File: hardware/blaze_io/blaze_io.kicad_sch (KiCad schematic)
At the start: 50 parts, among them J1 Conn_01x04, J2 Conn_01x04, J3 JTAG, Q1 AO4892, Q2 AO4892, SW1 SW_SPST, SW2 SW_SPDT, U1 TCAN1044VDDFR, U2 STM32H503KBUx

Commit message: Connected IO, wrote docs
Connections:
- net FET_A: now also U2.6 (PA0)
- net FET_A_SENSE: now also U2.10 (PA4)
- net FET_B: now also U2.7 (PA1)
- net FET_B_SENSE: now also U2.11 (PA5)
- net FET_C: now also U2.8 (PA2)
- net FET_C_SENSE: now also U2.12 (PA6)
- net FET_D: now also U2.9 (PA3)
- net FET_D_SENSE: now also U2.13 (PA7)
- no-connect marks 17 -> 11

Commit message: Updated IO title block
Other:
- company: (none) -> UCSC Rocket Team
- title: (none) -> Blaze IO
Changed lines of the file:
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@@
 	(generator_version "8.0")
 	(paper "A4")
+	(title_block
+		(title "Blaze IO")
+		(date "2024-09-19")
+		(rev "1")
+		(company "UCSC Rocket Team")
+		(comment 1 "Designed by Julian Barbera")
+	)

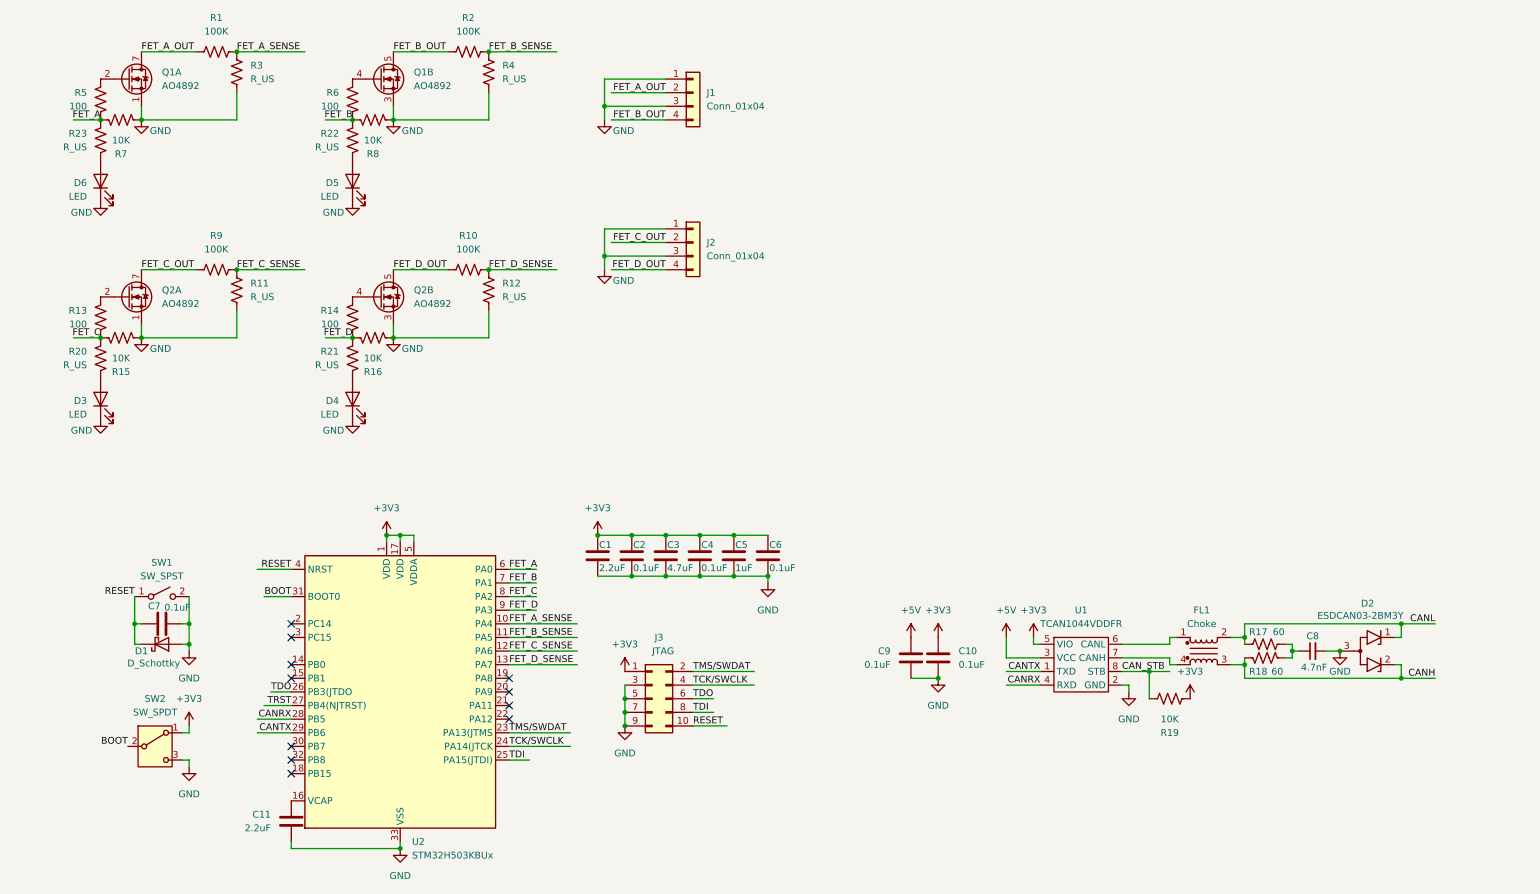
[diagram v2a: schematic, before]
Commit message: Added ARM AND gates to IO board
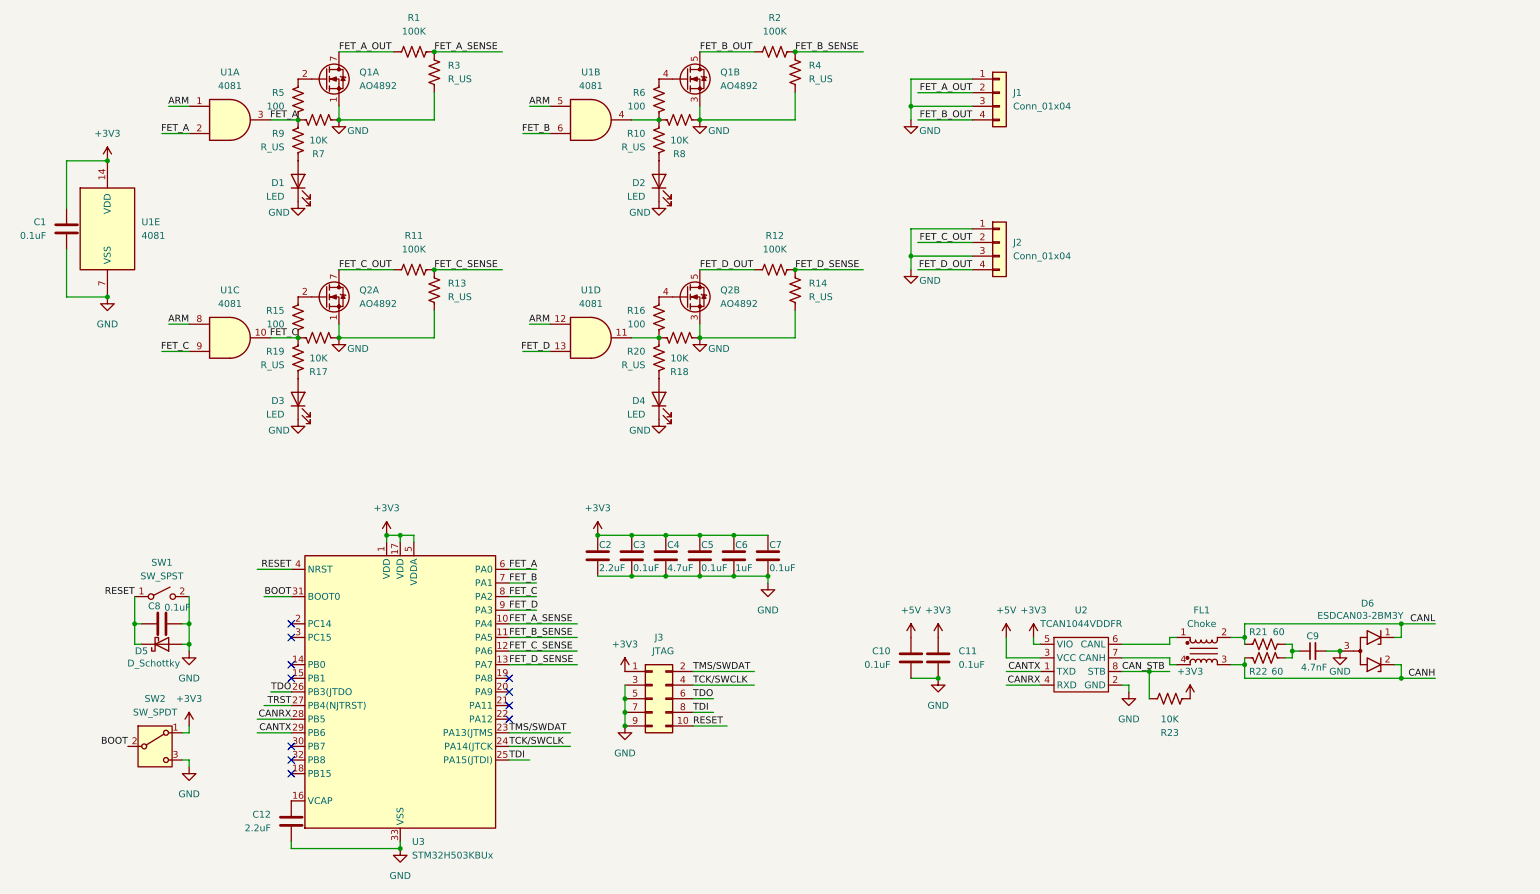
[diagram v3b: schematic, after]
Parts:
- added C1: 0.1uF, symbol Device:C
- added U1: 4081, symbol 4xxx:4081
- renumbered C9 to C10, C10 to C11, C11 to C12, C1 to C2, C2 to C3, C3 to C4, C4 to C5, C5 to C6, C6 to C7, C7 to C8, C8 to C9, D6 to D1, D5 to D2, D1 to D5, D2 to D6, R22 to R10, R9 to R11, R10 to R12, R11 to R13, R12 to R14, R13 to R15, R14 to R16, R15 to R17, R16 to R18, R20 to R19, R21 to R20, R17 to R21, R18 to R22, R19 to R23, R23 to R9, U1 to U2, U2 to U3
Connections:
- net +3V3: now also C1.1, U1.14 (VDD)
- net FET_A: now also U1.2, U1.3
- net FET_B: now also U1.6; no longer R10.1, R6.2, R8.1
- net FET_C: now also U1.10, U1.9
- net FET_D: now also U1.13; no longer R16.2, R18.1, R20.1
- net GND: now also C1.2, U1.7 (VSS)
- new net: R16.2, R18.1, R20.1, U1.11
- new net: R10.1, R6.2, R8.1, U1.4
- new net ARM: U1.1, U1.12, U1.5, U1.8
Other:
- moved on the sheet: D1, D2, D3, D4, J1, J2, Q1A, Q1B, Q2A, Q2B, R1, R10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

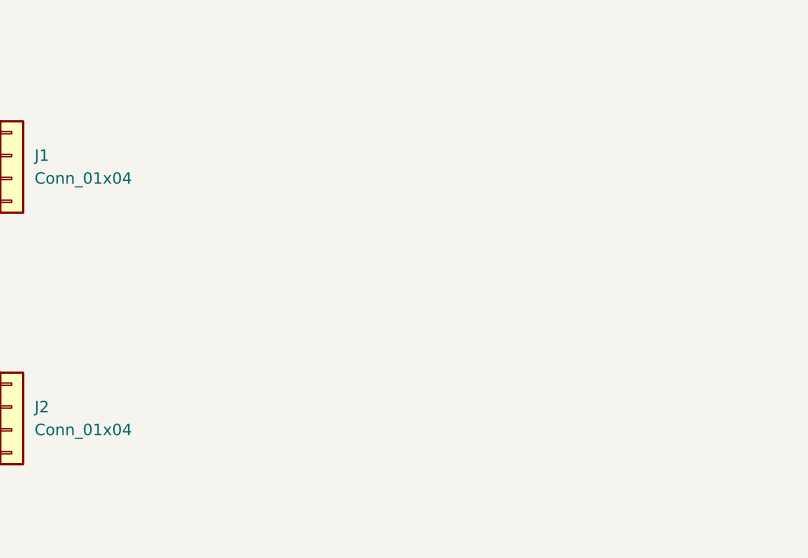
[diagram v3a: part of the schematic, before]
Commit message: Added servo outputs
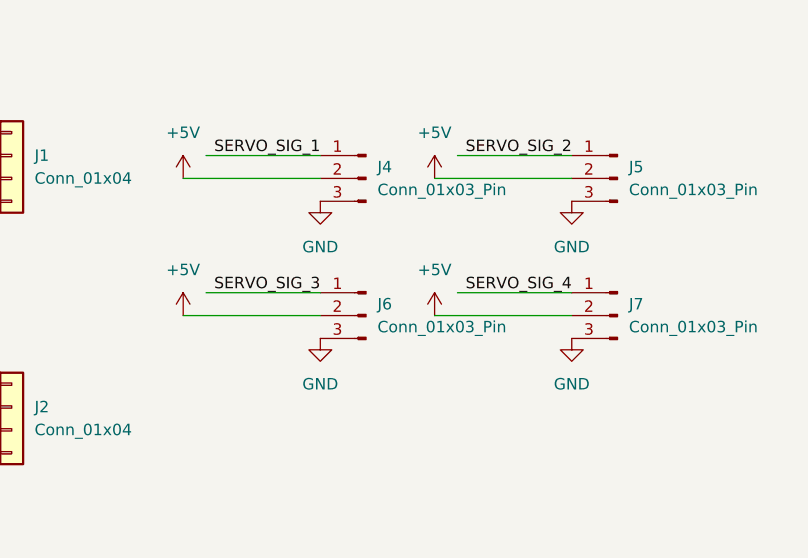
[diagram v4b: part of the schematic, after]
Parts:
- added J4, J5, J6, J7: Conn_01x03_Pin, symbol Connector:Conn_01x03_Pin
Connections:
- net +5V: now also J4.2 (Pin_2), J5.2 (Pin_2), J6.2 (Pin_2), J7.2 (Pin_2)
- net GND: now also J4.3 (Pin_3), J5.3 (Pin_3), J6.3 (Pin_3), J7.3 (Pin_3)
- new net SERVO_SIG_1: J4.1 (Pin_1)
- new net SERVO_SIG_2: J5.1 (Pin_1)
- new net SERVO_SIG_3: J6.1 (Pin_1)
- new net SERVO_SIG_4: J7.1 (Pin_1)

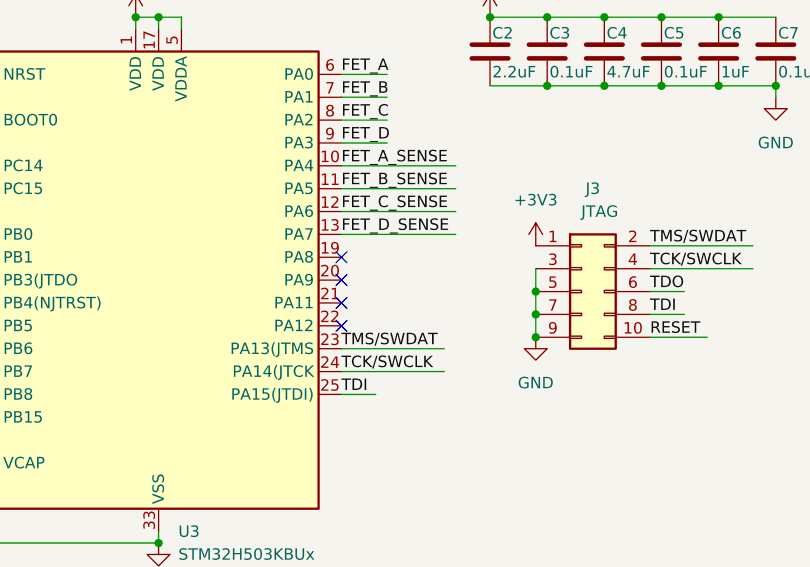
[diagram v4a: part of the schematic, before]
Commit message: Added PWM outputs to microcontroller
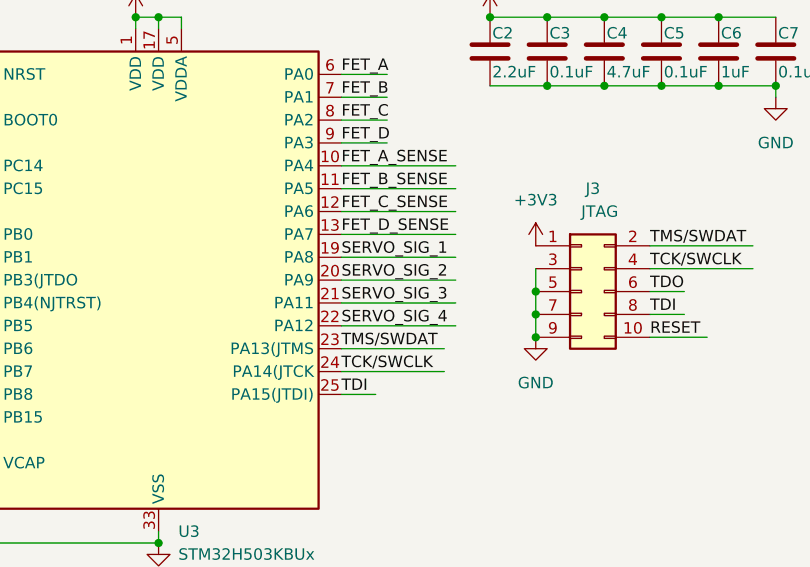
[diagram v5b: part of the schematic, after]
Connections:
- net SERVO_SIG_1: now also U3.19 (PA8)
- net SERVO_SIG_2: now also U3.20 (PA9)
- net SERVO_SIG_3: now also U3.21 (PA11)
- net SERVO_SIG_4: now also U3.22 (PA12)
- no-connect marks 11 -> 7

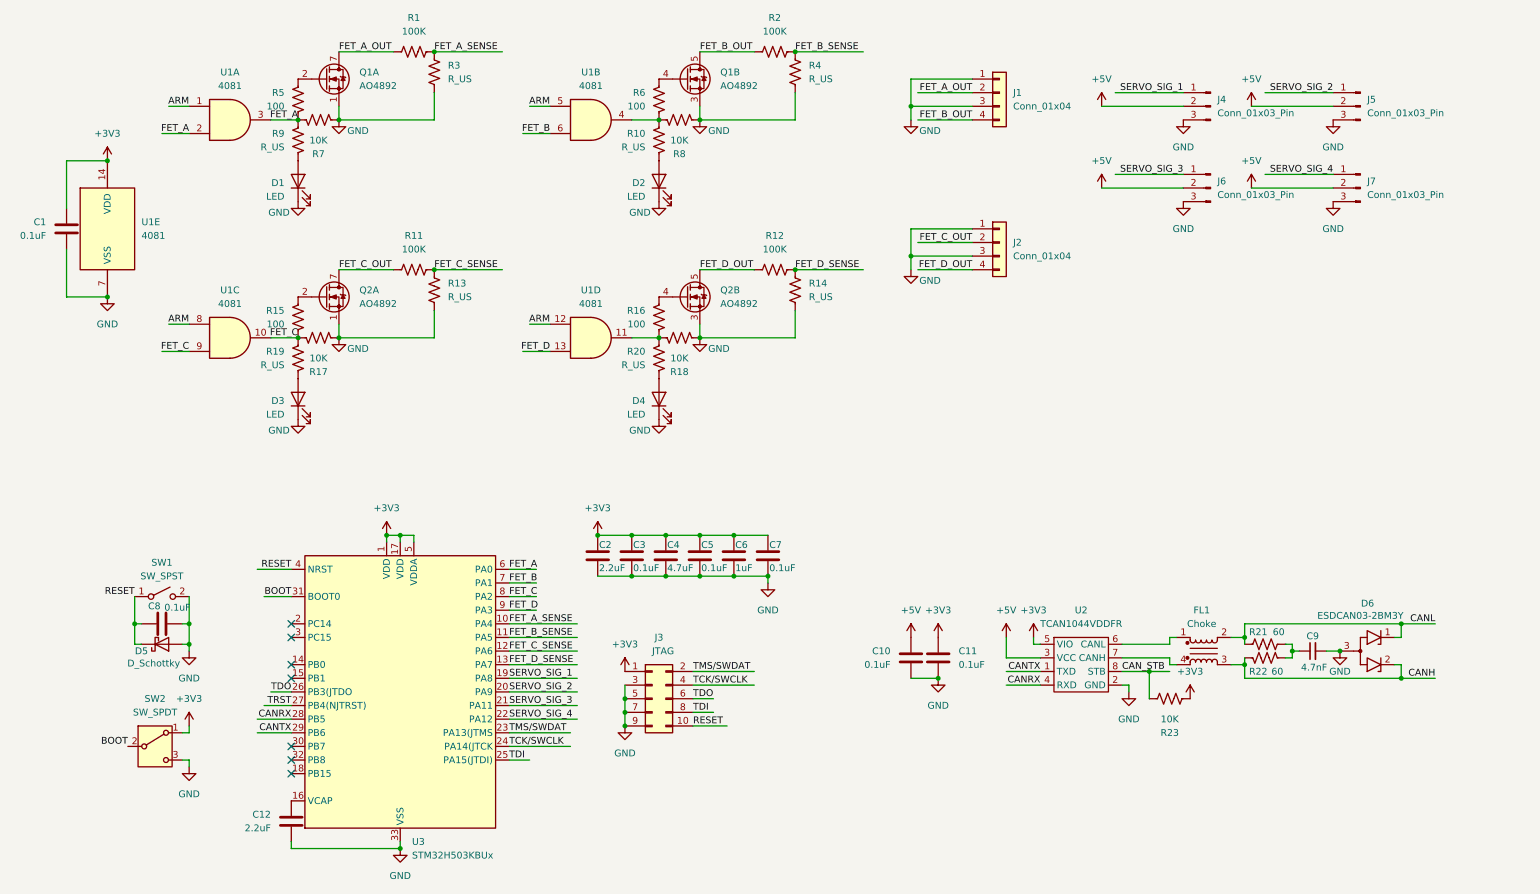
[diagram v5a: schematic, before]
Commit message: Removed audio, neopixel, can2 from interconnect
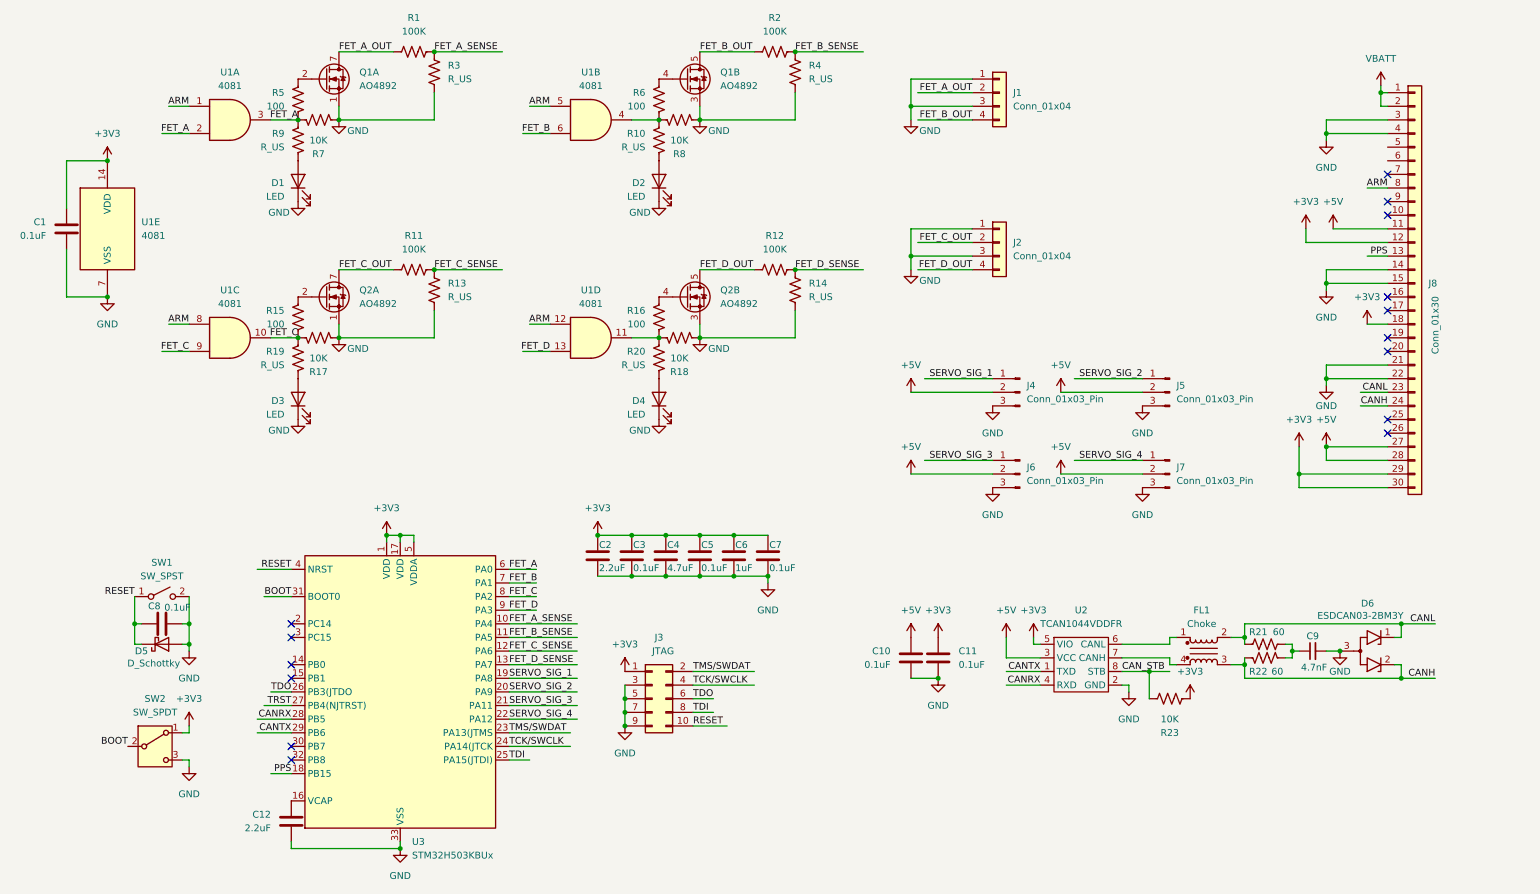
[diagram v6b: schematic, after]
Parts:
- added J8: Conn_01x30, symbol Connector_Generic:Conn_01x30
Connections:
- net +3V3: now also J8.12 (Pin_12), J8.18 (Pin_18), J8.29 (Pin_29), J8.30 (Pin_30)
- net +5V: now also J8.11 (Pin_11), J8.27 (Pin_27), J8.28 (Pin_28)
- net ARM: now also J8.8 (Pin_8)
- net CANH: now also J8.24 (Pin_24)
- net CANL: now also J8.23 (Pin_23)
- net GND: now also J8.14 (Pin_14), J8.15 (Pin_15), J8.21 (Pin_21), J8.22 (Pin_22), J8.3 (Pin_3), J8.4 (Pin_4)
- net PPS: now reaches U3.18 (PB15)
- net PPS: now also J8.13 (Pin_13)
- new net VBATT: J8.1 (Pin_1), J8.2 (Pin_2)
- no-connect marks 7 -> 15
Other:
- moved on the sheet: J4, J5, J6, J7

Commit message: IO Footprint Assignments
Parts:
- C1, C10, C11, C12, C2, C3, C4, C5, C6, C7, C8, C9: footprint (none) -> Capacitor_SMD:C_0603_1608Metric
- D1, D2, D3, D4: footprint (none) -> LED_SMD:LED_0603_1608Metric
- D5: footprint (none) -> Diode_SMD:D_0603_1608Metric
- J3: footprint (none) -> Connector_PinHeader_1.00mm:PinHeader_2x05_P1.00mm_Vertical_SMD
- J8: footprint (none) -> DF17:HRS_DF17_1.0H_-30DP-0.5V_57_
- R1, R10, R11, R12, R13, R14, R15, R16, R17, R18, R19, R2, R20, R21, R22, R23, R3, R4, R5, R6, R7, R8, R9: footprint (none) -> Resistor_SMD:R_0603_1608Metric
- SW1: footprint (none) -> Button_Switch_SMD:SW_SPST_B3U-1000P
- SW2: footprint (none) -> Button_Switch_SMD:Nidec_Copal_CAS-120A
- U2: footprint (none) -> Package_SON:Texas_VSON-HR-8_1.5x2mm_P0.5mm

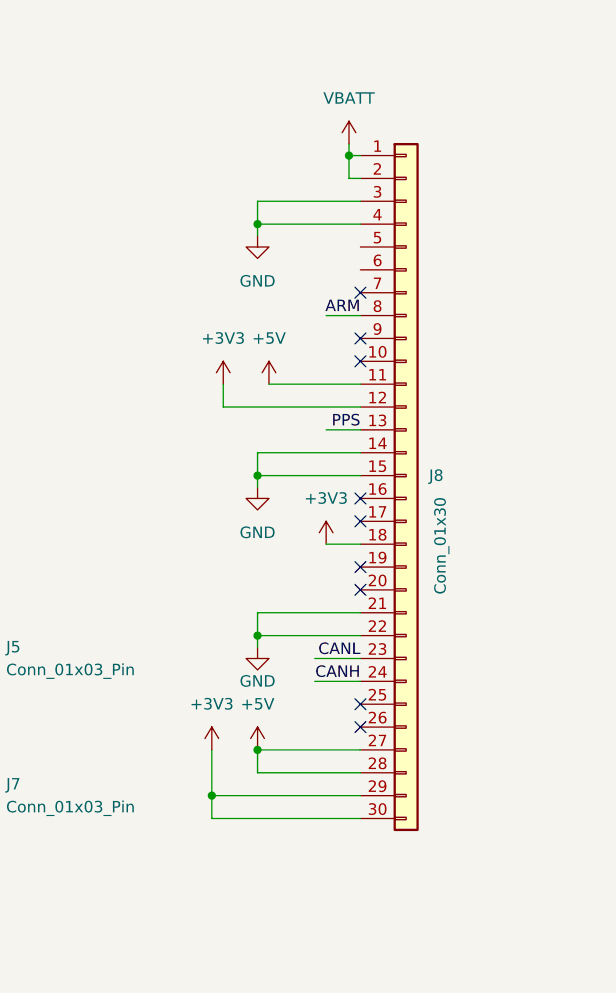
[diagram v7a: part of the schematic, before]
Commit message: Added mirror interconnect and PCB to io
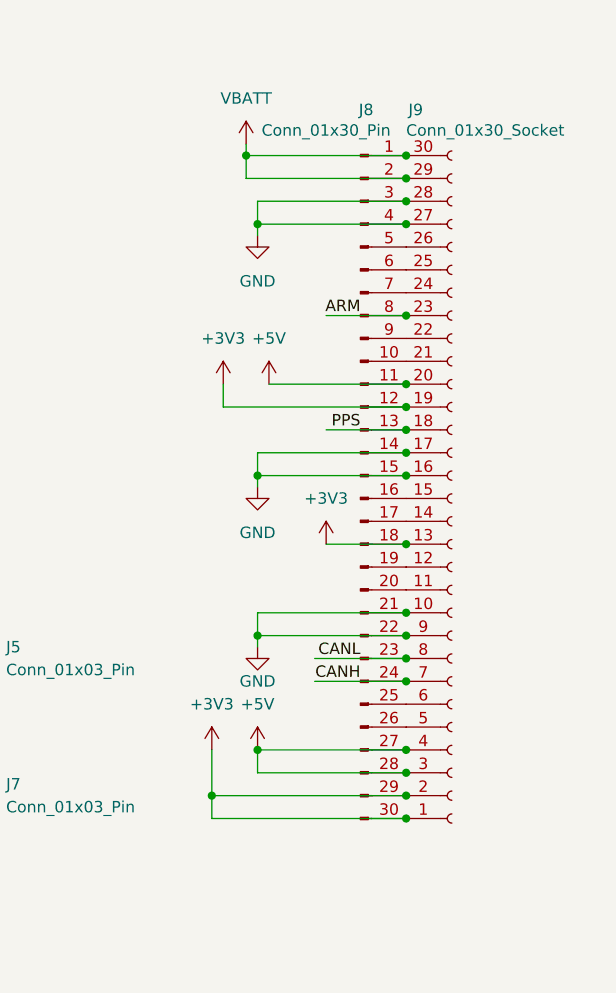
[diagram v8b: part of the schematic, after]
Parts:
- removed J8: Conn_01x30, DF17:HRS_DF17_1.0H_-30DP-0.5V_57_, symbol Connector_Generic:Conn_01x30
- added J8: Conn_01x30_Pin, Blaze_Library:HRS_DF17_1.0H_-30DP-0.5V_57_, symbol Connector:Conn_01x30_Pin
- added J9: Conn_01x30_Socket, Blaze_Library:HRS_DF17_1.0H_-30DP-0.5V_57_, symbol Connector:Conn_01x30_Socket
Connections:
- net +3V3: now also J8.12 (Pin_12), J8.18 (Pin_18), J8.29 (Pin_29), J8.30 (Pin_30), J9.1 (Pin_1), J9.13 (Pin_13), J9.19 (Pin_19), J9.2 (Pin_2)
- net +5V: now also J8.11 (Pin_11), J8.27 (Pin_27), J8.28 (Pin_28), J9.20 (Pin_20), J9.3 (Pin_3), J9.4 (Pin_4)
- net ARM: now also J8.8 (Pin_8), J9.23 (Pin_23)
- net CANH: now also J8.24 (Pin_24), J9.7 (Pin_7)
- net CANL: now also J8.23 (Pin_23), J9.8 (Pin_8)
- net GND: now also J8.14 (Pin_14), J8.15 (Pin_15), J8.21 (Pin_21), J8.22 (Pin_22), J8.3 (Pin_3), J8.4 (Pin_4), J9.10 (Pin_10), J9.16 (Pin_16), J9.17 (Pin_17), J9.27 (Pin_27), J9.28 (Pin_28), J9.9 (Pin_9)
- net PPS: now also J8.13 (Pin_13), J9.18 (Pin_18)
- net VBATT: now also J8.1 (Pin_1), J8.2 (Pin_2), J9.29 (Pin_29), J9.30 (Pin_30)
- new net: J8.10 (Pin_10), J9.21 (Pin_21)
- new net: J8.16 (Pin_16), J9.15 (Pin_15)
- new net: J8.17 (Pin_17), J9.14 (Pin_14)
- new net: J8.19 (Pin_19), J9.12 (Pin_12)
- new net: J8.20 (Pin_20), J9.11 (Pin_11)
- new net: J8.25 (Pin_25), J9.6 (Pin_6)
- new net: J8.26 (Pin_26), J9.5 (Pin_5)
- new net: J8.5 (Pin_5), J9.26 (Pin_26)
- new net: J8.6 (Pin_6), J9.25 (Pin_25)
- new net: J8.7 (Pin_7), J9.24 (Pin_24)
- new net: J8.9 (Pin_9), J9.22 (Pin_22)
- no-connect marks 15 -> 6
